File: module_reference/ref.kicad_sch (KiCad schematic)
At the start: 77 parts, among them Q201 BDP949, U201 ADR1000, U202 OPA2140, U203 ADA4523-1

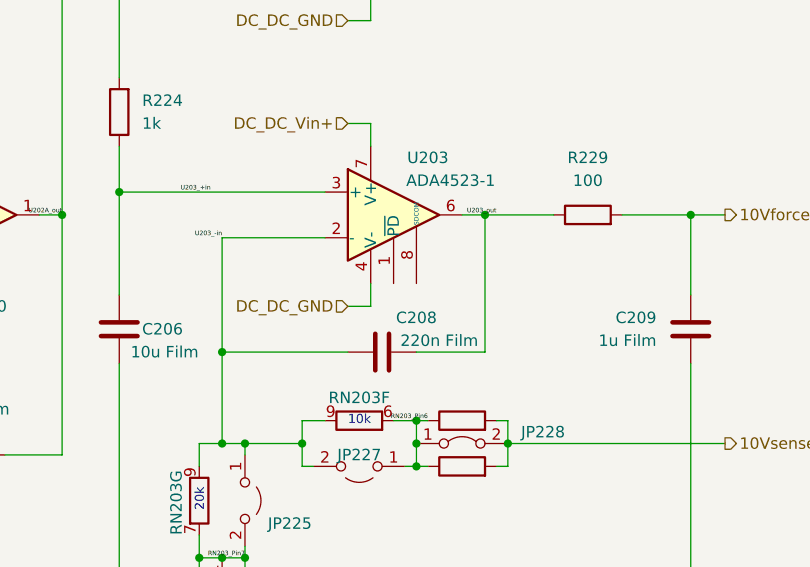
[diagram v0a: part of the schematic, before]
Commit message: backplane connector changes
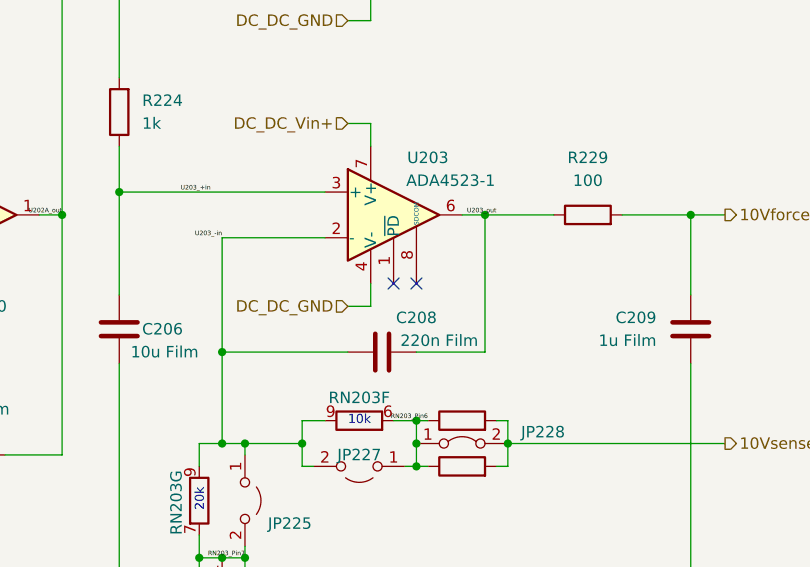
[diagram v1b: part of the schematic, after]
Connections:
- no-connect marks 0 -> 2
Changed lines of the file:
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@@
   (junction (at 107.95 106.68) (diameter 0) (color 0 0 0 0)
   )
+  (no_connect (at 223.52 76.2))
+  (no_connect (at 220.98 76.2))
   (wire (pts (xy 218.44 76.2) (xy 218.44 78.74))
     (stroke (width 0) (type default) (color 0 0 0 0))

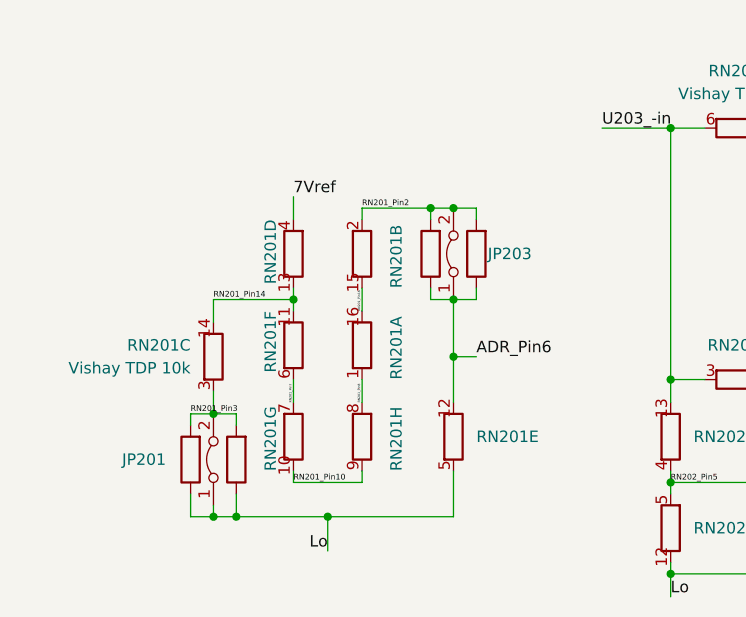
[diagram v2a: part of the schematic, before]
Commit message: started Rev. 0.4 with better 1k/12k divider
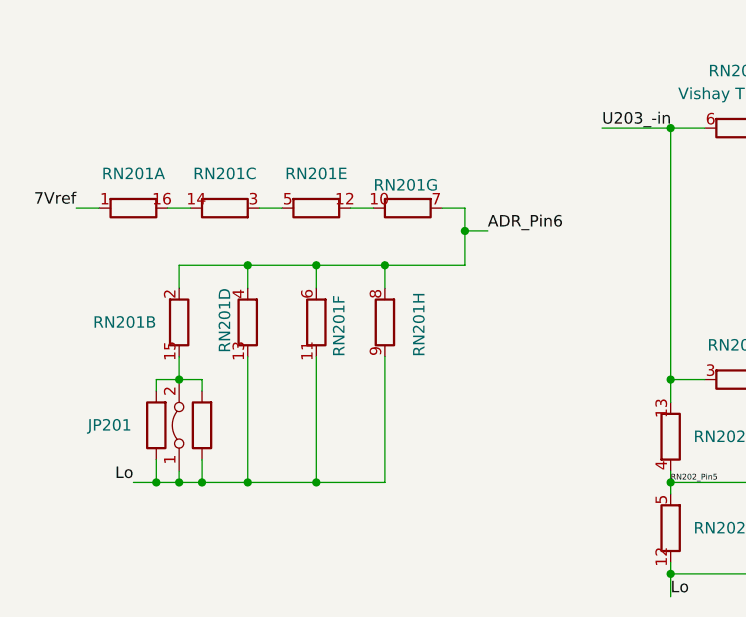
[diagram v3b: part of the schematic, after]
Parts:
- removed JP203: Jumper_2_Bridged, Jumper:SolderJumper-2_P1.3mm_Bridged_RoundedPad1.0x1.5mm, symbol Jumper:Jumper_2_Bridged
- removed R203: 0, Crystal:Crystal_HC52-U_Vertical, symbol Device:R
- removed R205: 0, Resistor_SMD:R_0805_2012Metric, symbol Device:R
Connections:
- net RN201_Pin2 is gone; now on net ADR_Pin6: RN201.2 (R2.1)
- net RN201_Pin7 is gone; now on net ADR_Pin6: RN201.6 (R6.1), RN201.7 (R7.1)
- net 7Vref: now also RN201.1 (R1.1); no longer RN201.4 (R4.1)
- net ADR_Pin6: now also RN201.4 (R4.1), RN201.8 (R8.1); no longer RN201.12 (R5.2)
- net Lo: now also RN201.11 (R6.2), RN201.13 (R4.2), RN201.9 (R8.2); no longer RN201.5 (R5.1)
- net RN201_Pin10: no longer names the net of RN201.10 (R7.2)
- net RN201_Pin10: now also RN201.12 (R5.2); no longer RN201.9 (R8.2)
- removed net RN201_Pin14: RN201.11 (R6.2), RN201.13 (R4.2), RN201.14 (R3.2)
- net RN201_Pin16: no longer names the net of RN201.15 (R2.2)
- net RN201_Pin16: now also JP201.2 (B), R201.2, R202.2; no longer RN201.16 (R1.2)
- removed net RN201_Pin3: JP201.2 (B), R201.2, R202.2, RN201.3 (R3.1)
- removed net RN201_Pin8: RN201.1 (R1.1), RN201.8 (R8.1)
- new net: RN201.3 (R3.1), RN201.5 (R5.1)
- new net: RN201.14 (R3.2), RN201.16 (R1.2)
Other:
- moved on the sheet: JP201, RN201A, RN201B, RN201C, RN201D, RN201E, RN201F, RN201G, RN201H

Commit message: rev 0.4 layout step
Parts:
- removed Q201: BDP949, Package_TO_SOT_SMD:SOT-223-3_TabPin2, symbol Device:Q_NPN_BCE
- added Q201: BD135, Package_TO_SOT_THT:TO-126-3_Vertical, symbol Transistor_BJT:BD135
- NT201: footprint NetTie:NetTie-2_SMD_Pad0.5mm -> NetTie:NetTie-2_SMD_Pad2.0mm
- renumbered JP204 to JP202, JP205 to JP203, JP206 to JP204, JP207 to JP205, JP208 to JP206, JP209 to JP207, JP210 to JP208, JP211 to JP209, JP212 to JP210, JP213 to JP211, JP214 to JP212, JP215 to JP213, JP216 to JP214, JP217 to JP215, JP218 to JP216, JP219 to JP217, JP220 to JP218, JP221 to JP219, JP222 to JP220, JP223 to JP221, JP224 to JP222, JP225 to JP223, JP226 to JP224, JP227 to JP225, JP228 to JP226, JP229 to JP227, R204 to R203, R206 to R204, R207 to R205, R208 to R206, R209 to R207, R210 to R208, R211 to R209, R212 to R210, R213 to R211, R214 to R212, R215 to R213, R216 to R214, R217 to R215, R218 to R216, R219 to R217, R220 to R218, R221 to R219, R222 to R220, R223 to R221, R224 to R222, R225 to R223, R226 to R224, R227 to R225, R228 to R226, R229 to R227
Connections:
- net DC_DC_Vin+: now also Q201.2 (C)
- net Q201_base: now also Q201.3 (B)
- net heater+: now also Q201.1 (E)
- net RN201_Pin10: now reaches RN201.10 (R7.2), RN201.12 (R5.2)
- net RN201_Pin15: now reaches JP201.2 (B), R201.2, R202.2, RN201.15 (R2.2)
- net RN201_Pin5: now reaches RN201.3 (R3.1), RN201.5 (R5.1)
- net RN201_Pin14: now reaches RN201.14 (R3.2), RN201.16 (R1.2)

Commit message: Battery module Rev 0.2
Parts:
- added JP?: Jumper_2_Bridged, Jumper:SolderJumper-2_P1.3mm_Bridged_RoundedPad1.0x1.5mm, symbol Jumper:Jumper_2_Bridged
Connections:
- net RN202_Pin14: now also JP?.2 (B)
- net RN202_Pin2: now also JP?.1 (A)
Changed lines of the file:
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@@
+    (stroke (width 0) (type default) (color 0 0 0 0))
+  )
+  (wire (pts (xy 114.3 167.64) (xy 115.57 167.64))
     (stroke (width 0) (type default) (color 0 0 0 0))
   )
@@
     (stroke (width 0) (type default) (color 0 0 0 0))
   )
+  (wire (pts (xy 115.57 162.56) (xy 115.57 167.64))
+    (stroke (width 0) (type default) (color 0 0 0 0))
+  )
   (wire (pts (xy 110.49 106.68) (xy 110.49 107.95))
     (stroke (width 0) (type default) (color 0 0 0 0))
@@
     (stroke (width 0) (type default) (color 0 0 0 0))
   )
+  (wire (pts (xy 102.87 167.64) (xy 104.14 167.64))
+    (stroke (width 0) (type default) (color 0 0 0 0))
+  )
   (wire (pts (xy 35.56 143.51) (xy 33.02 143.51))
     (stroke (width 0) (type default) (color 0 0 0 0))
@@
   )
   (wire (pts (xy 130.81 162.56) (xy 140.97 162.56))
+    (stroke (width 0) (type default) (color 0 0 0 0))
+  )
+  (wire (pts (xy 102.87 162.56) (xy 102.87 167.64))
     (stroke (width 0) (type default) (color 0 0 0 0))
   )
@@
       (effects (font (size 1.27 1.27)) hide)
     )
+    (pin "1")
+    (pin "2")
+  )
+  (symbol (lib_id "Jumper:Jumper_2_Bridged") (at 109.22 167.64 180) (unit 1)
+    (in_bom no) (on_board yes) (fields_autoplaced)
+    (property "Reference" "JP?" (id 0) (at 109.22 165.1 0))
+    (property "Value" "Jumper_2_Bridged" (id 1) (at 109.22 171.45 0)
+      (effects (font (size 1.27 1.27)) hide)
+    )
+    (property "Footprint" "Jumper:SolderJumper-2_P1.3mm_Bridged_RoundedPad1.0x1.5mm" (id 2) (at 109.22 167.64 0)
+      (effects (font (size 1.27 1.27)) hide)
+    )
+    (property "Datasheet" "~" (id 3) (at 109.22 167.64 0)
+      (effects (font (size 1.27 1.27)) hide)
+    )

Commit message: asdf
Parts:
- removed JP?: Jumper_2_Bridged, Jumper:SolderJumper-2_P1.3mm_Bridged_RoundedPad1.0x1.5mm, symbol Jumper:Jumper_2_Bridged
- renumbered JP204 to JP205, JP205 to JP206, JP206 to JP207, JP207 to JP208, JP208 to JP209, JP209 to JP210, JP210 to JP211, JP211 to JP212, JP212 to JP213, JP213 to JP214, JP214 to JP215, JP215 to JP216, JP216 to JP217, JP217 to JP218, JP218 to JP219, JP219 to JP220, JP220 to JP221, JP221 to JP222, JP222 to JP223, JP223 to JP224, JP224 to JP225, JP225 to JP226, JP226 to JP227, JP227 to JP228
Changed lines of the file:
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@@
-    (stroke (width 0) (type default) (color 0 0 0 0))
-  )
-  (wire (pts (xy 114.3 167.64) (xy 115.57 167.64))
     (stroke (width 0) (type default) (color 0 0 0 0))
   )
@@
     (stroke (width 0) (type default) (color 0 0 0 0))
   )
-  (wire (pts (xy 115.57 162.56) (xy 115.57 167.64))
-    (stroke (width 0) (type default) (color 0 0 0 0))
-  )
   (wire (pts (xy 110.49 106.68) (xy 110.49 107.95))
     (stroke (width 0) (type default) (color 0 0 0 0))
@@
     (stroke (width 0) (type default) (color 0 0 0 0))
   )
-  (wire (pts (xy 102.87 167.64) (xy 104.14 167.64))
-    (stroke (width 0) (type default) (color 0 0 0 0))
-  )
   (wire (pts (xy 35.56 143.51) (xy 33.02 143.51))
     (stroke (width 0) (type default) (color 0 0 0 0))
@@
   )
   (wire (pts (xy 130.81 162.56) (xy 140.97 162.56))
-    (stroke (width 0) (type default) (color 0 0 0 0))
-  )
-  (wire (pts (xy 102.87 162.56) (xy 102.87 167.64))
     (stroke (width 0) (type default) (color 0 0 0 0))
   )
@@
   (symbol (lib_id "Jumper:Jumper_2_Open") (at 123.19 184.15 180) (unit 1)
     (in_bom no) (on_board yes) (fields_autoplaced)
-    (property "Reference" "JP212" (id 0) (at 123.19 181.61 0))
+    (property "Reference" "JP213" (id 0) (at 123.19 181.61 0))
     (property "Value" "Jumper_2_Open" (id 1) (at 121.9201 186.69 90)
       (effects (font (size 1.27 1.27)) (justify left) hide)
@@
   (symbol (lib_id "Jumper:Jumper_2_Open") (at 118.11 59.69 270) (unit 1)
     (in_bom no) (on_board yes)
-    (property "Reference" "JP207" (id 0) (at 113.03 59.69 90)
+    (property "Reference" "JP208" (id 0) (at 113.03 59.69 90)
       (effects (font (size 1.27 1.27)) (justify left))
     )
@@
   (symbol (lib_id "Jumper:Jumper_2_Open") (at 110.49 100.33 270) (unit 1)
     (in_bom no) (on_board yes)
-    (property "Reference" "JP205" (id 0) (at 113.03 100.33 90)
+    (property "Reference" "JP206" (id 0) (at 113.03 100.33 90)
       (effects (font (size 1.27 1.27)) (justify left))
     )
@@
   (symbol (lib_id "Jumper:Jumper_2_Bridged") (at 228.6 93.98 0) (unit 1)
     (in_bom no) (on_board yes)
-    (property "Reference" "JP226" (id 0) (at 240.03 92.71 0)
+    (property "Reference" "JP227" (id 0) (at 240.03 92.71 0)
       (effects (font (size 1.27 1.27)) (justify right))
     )
@@
     (pin "2")
   )
-  (symbol (lib_id "Jumper:Jumper_2_Bridged") (at 109.22 167.64 180) (unit 1)
-    (in_bom no) (on_board yes) (fields_autoplaced)
-    (property "Reference" "JP?" (id 0) (at 109.22 165.1 0))
-    (property "Value" "Jumper_2_Bridged" (id 1) (at 109.22 171.45 0)
-      (effects (font (size 1.27 1.27)) hide)
-    )
-    (property "Footprint" "Jumper:SolderJumper-2_P1.3mm_Bridged_RoundedPad1.0x1.5mm" (id 2) (at 109.22 167.64 0)
-      (effects (font (size 1.27 1.27)) hide)
-    )
-    (property "Datasheet" "~" (id 3) (at 109.22 167.64 0)
-      (effects (font (size 1.27 1.27)) hide)
-    )
-    (pin "1")
-    (pin "2")
-  )
   (symbol (lib_id "Jumper:Jumper_2_Bridged") (at 201.93 111.76 270) (unit 1)
     (in_bom no) (on_board yes)
-    (property "Reference" "JP222" (id 0) (at 205.74 119.38 90)
+    (property "Reference" "JP223" (id 0) (at 205.74 119.38 90)
       (effects (font (size 1.27 1.27)) (justify right))
     )
@@
   (symbol (lib_id "Jumper:Jumper_2_Open") (at 199.39 139.7 270) (unit 1)
     (in_bom no) (on_board yes)
-    (property "Reference" "JP221" (id 0) (at 201.93 142.24 90)
+    (property "Reference" "JP222" (id 0) (at 201.93 142.24 90)
       (effects (font (size 1.27 1.27)) (justify left))
     )
@@
   (symbol (lib_id "Jumper:Jumper_2_Open") (at 217.17 96.52 180) (unit 1)
     (in_bom no) (on_board yes)
-    (property "Reference" "JP225" (id 0) (at 217.17 95.25 0))
+    (property "Reference" "JP226" (id 0) (at 217.17 95.25 0))
     (property "Value" "Jumper_2_Open" (id 1) (at 217.17 96.52 0)
       (effects (font (size 1.27 1.27)) hide)
@@
   (symbol (lib_id "Jumper:Jumper_2_Open") (at 208.28 154.94 270) (unit 1)
     (in_bom no) (on_board yes)
-    (property "Reference" "JP224" (id 0) (at 210.82 157.48 90)
+    (property "Reference" "JP225" (id 0) (at 210.82 157.48 90)
       (effects (font (size 1.27 1.27)) (justify left))
     )
@@
   (symbol (lib_id "Jumper:Jumper_2_Bridged") (at 130.81 48.26 90) (unit 1)
     (in_bom no) (on_board yes)
-    (property "Reference" "JP213" (id 0) (at 128.27 40.64 90)
+    (property "Reference" "JP214" (id 0) (at 128.27 40.64 90)
       (effects (font (size 1.27 1.27)) (justify right))
     )
@@
   (symbol (lib_id "Jumper:Jumper_2_Bridged") (at 130.81 142.24 270) (unit 1)
     (in_bom no) (on_board yes) (fields_autoplaced)
-    (property "Reference" "JP214" (id 0) (at 133.35 142.2399 90)
+    (property "Reference" "JP215" (id 0) (at 133.35 142.2399 90)
       (effects (font (size 1.27 1.27)) (justify left))
     )
@@
   (symbol (lib_id "Jumper:Jumper_2_Open") (at 115.57 142.24 270) (unit 1)
     (in_bom no) (on_board yes) (fields_autoplaced)
-    (property "Reference" "JP206" (id 0) (at 114.3 142.2399 90)
+    (property "Reference" "JP207" (id 0) (at 114.3 142.2399 90)
       (effects (font (size 1.27 1.27)) (justify right))
     )
@@
   (symbol (lib_id "Jumper:Jumper_2_Open") (at 134.62 100.33 90) (unit 1)
     (in_bom no) (on_board yes)
-    (property "Reference" "JP217" (id 0) (at 135.89 100.33 90)
+    (property "Reference" "JP218" (id 0) (at 135.89 100.33 90)
       (effects (font (size 1.27 1.27)) (justify right))
     )
@@
   (symbol (lib_id "Jumper:Jumper_2_Bridged") (at 243.84 139.7 270) (unit 1)
     (in_bom no) (on_board yes)
-    (property "Reference" "JP227" (id 0) (at 246.38 138.43 0)
+    (property "Reference" "JP228" (id 0) (at 246.38 138.43 0)
       (effects (font (size 1.27 1.27)) (justify left))
     )
@@
   (symbol (lib_id "Jumper:Jumper_2_Open") (at 133.35 59.69 270) (unit 1)
     (in_bom no) (on_board yes)
-    (property "Reference" "JP216" (id 0) (at 137.16 57.15 0)
+    (property "Reference" "JP217" (id 0) (at 137.16 57.15 0)
       (effects (font (size 1.27 1.27)) (justify left))
     )
@@
   (symbol (lib_id "Jumper:Jumper_2_Bridged") (at 123.19 162.56 180) (unit 1)
     (in_bom no) (on_board yes) (fields_autoplaced)
-    (property "Reference" "JP210" (id 0) (at 123.19 160.02 0))
+    (property "Reference" "JP211" (id 0) (at 123.19 160.02 0))
     (property "Value" "Jumper_2_Bridged" (id 1) (at 123.19 166.37 0)
       (effects (font (size 1.27 1.27)) hide)
@@
   (symbol (lib_id "Jumper:Jumper_2_Open") (at 123.19 173.99 180) (unit 1)
     (in_bom no) (on_board yes) (fields_autoplaced)
-    (property "Reference" "JP211" (id 0) (at 123.19 171.45 0))
+    (property "Reference" "JP212" (id 0) (at 123.19 171.45 0))
     (property "Value" "Jumper_2_Open" (id 1) (at 121.9201 176.53 90)
       (effects (font (size 1.27 1.27)) (justify left) hide)
@@
   (symbol (lib_id "Jumper:Jumper_2_Bridged") (at 132.08 111.76 270) (unit 1)
     (in_bom no) (on_board yes)
-    (property "Reference" "JP215" (id 0) (at 135.89 119.38 90)
+    (property "Reference" "JP216" (id 0) (at 135.89 119.38 90)
       (effects (font (size 1.27 1.27)) (justify right))
     )
@@
   (symbol (lib_id "Jumper:Jumper_2_Open") (at 110.49 74.93 270) (unit 1)
     (in_bom no) (on_board yes)
-    (property "Reference" "JP204" (id 0) (at 114.3 72.39 0)
+    (property "Reference" "JP205" (id 0) (at 114.3 72.39 0)
       (effects (font (size 1.27 1.27)) (justify left))
     )
@@
   (symbol (lib_id "Jumper:Jumper_2_Open") (at 204.47 100.33 270) (unit 1)
     (in_bom no) (on_board yes)
-    (property "Reference" "JP223" (id 0) (at 207.01 102.87 90)
+    (property "Reference" "JP224" (id 0) (at 207.01 102.87 90)
       (effects (font (size 1.27 1.27)) (justify left))
     )
@@
   (symbol (lib_id "Jumper:Jumper_2_Bridged") (at 154.94 48.26 90) (unit 1)
     (in_bom no) (on_board yes)
-    (property "Reference" "JP220" (id 0) (at 158.75 48.26 90)
+    (property "Reference" "JP221" (id 0) (at 158.75 48.26 90)
       (effects (font (size 1.27 1.27)) (justify right))
     )
@@
   (symbol (lib_id "Jumper:Jumper_2_Open") (at 151.13 142.24 270) (unit 1)
     (in_bom no) (on_board yes) (fields_autoplaced)
-    (property "Reference" "JP219" (id 0) (at 153.67 142.2399 90)
+    (property "Reference" "JP220" (id 0) (at 153.67 142.2399 90)
       (effects (font (size 1.27 1.27)) (justify left))
     )
@@
   (symbol (lib_id "Jumper:Jumper_2_Bridged") (at 140.97 142.24 270) (unit 1)
     (in_bom no) (on_board yes) (fields_autoplaced)
-    (property "Reference" "JP218" (id 0) (at 143.51 142.2399 90)
+    (property "Reference" "JP219" (id 0) (at 143.51 142.2399 90)
       (effects (font (size 1.27 1.27)) (justify left))
     )
@@
   (symbol (lib_id "Jumper:Jumper_2_Bridged") (at 120.65 48.26 90) (unit 1)
     (in_bom no) (on_board yes)
-    (property "Reference" "JP208" (id 0) (at 118.11 40.64 90)
+    (property "Reference" "JP209" (id 0) (at 118.11 40.64 90)
       (effects (font (size 1.27 1.27)) (justify right))
     )
@@
   (symbol (lib_id "Jumper:Jumper_2_Bridged") (at 123.19 134.62 180) (unit 1)
     (in_bom no) (on_board yes)
-    (property "Reference" "JP209" (id 0) (at 123.19 137.16 0))
+    (property "Reference" "JP210" (id 0) (at 123.19 137.16 0))
     (property "Value" "Jumper_2_Bridged" (id 1) (at 123.19 138.43 0)
       (effects (font (size 1.27 1.27)) hide)

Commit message: Reference board Rev 0.5 schematic
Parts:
- removed JP201, JP210, JP211, JP215, JP219: Jumper_2_Bridged, Jumper:SolderJumper-2_P1.3mm_Bridged_RoundedPad1.0x1.5mm, symbol Jumper:Jumper_2_Bridged
- removed JP212, JP213, JP222, JP225: Jumper_2_Open, Jumper:SolderJumper-2_P1.3mm_Open_RoundedPad1.0x1.5mm, symbol Jumper:Jumper_2_Open
- added J201, J202, J203, J204, J205, J206, J207, J208: Conn_01x01, Connector_Wire:SolderWire-0.1sqmm_1x01_D0.4mm_OD1mm, symbol Connector_Generic:Conn_01x01
- added JP201, JP214: Jumper_2_Open, Jumper:SolderJumper-2_P1.3mm_Open_RoundedPad1.0x1.5mm, symbol Jumper:Jumper_2_Open
- added JP218, JP220: Jumper_2_Bridged, Jumper:SolderJumper-2_P1.3mm_Bridged_RoundedPad1.0x1.5mm, symbol Jumper:Jumper_2_Bridged
- added R218: 30k, Resistor_SMD:R_0805_2012Metric, symbol Device:R
- added R222, R224: DNP, Resistor_SMD:R_0805_2012Metric, symbol Device:R
- added R223, R225: DNP, Crystal:Crystal_HC52-U_Vertical, symbol Device:R
- R201: footprint Crystal:Crystal_HC52-U_Vertical -> Resistor_SMD:R_0805_2012Metric
- R202: footprint Resistor_SMD:R_0805_2012Metric -> Crystal:Crystal_HC52-U_Vertical
- R221: renamed from R218; value 0 -> DNP
- R226: renamed from R220; value 0 -> DNP
- renumbered JP205 to JP204, JP206 to JP205, JP208 to JP206, JP209 to JP207, JP214 to JP208, JP216 to JP209, JP217 to JP210, JP218 to JP211, JP207 to JP212, JP221 to JP213, JP220 to JP215, JP223 to JP216, JP224 to JP217, JP226 to JP219, JP227 to JP221, JP228 to JP222, R221 to R220, R222 to R227, R223 to R228, R224 to R229, R225 to R230, R226 to R231, R227 to R232
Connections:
- net RN202_Pin5 is gone; now on net U203_-in: RN202.4 (R4.1), RN202.5 (R5.1)
- net RN202_Pin8 is gone; now on net U203_-in: RN202.8 (R8.1)
- net 10Vsense: now also RN202.10 (R7.2), RN202.12 (R5.2), RN202.13 (R4.2), RN202.15 (R2.2), RN202.16 (R1.2), JP214.1 (A); no longer JP212.1 (A), RN202.7 (R7.1)
- net 7Vref: now also JP218.1 (A)
- net ADR_Pin4: now also R218.1; no longer C205.2, U202.2 (-)
- net ADR_Pin5: now also R222.1, R223.2
- net ADR_Pin6: now also R201.1, R202.1, RN201.5 (R5.1), JP201.2 (B); no longer RN201.2 (R2.1), RN201.4 (R4.1)
- net RN201_Pin14: now also J201.1 (Pin_1); no longer RN201.16 (R1.2)
- net RN201_Pin15: now also RN201.16 (R1.2); no longer R201.2, R202.2
- net RN204_Pin11: now also JP220.2 (B)
- net RN204_Pin16: now also JP218.2 (B), JP220.1 (A)
- net U202A_out: now also R222.2, R223.1, R224.2, R225.1
- net U203_-in: now also JP212.1 (A), RN202.2 (R2.1), RN202.7 (R7.1); no longer RN202.13 (R4.2)
- net JP211_Pin1 renamed ADR_Pin7
- net ADR_Pin7: now also C203.1, C204.1, C206.2, C209.1, JP203.2 (B), JP209.2 (B), JP216.2 (B), NT201.2, R207.2, R209.2, R213.2, R215.2, R228.2, R229.2, RN201.10 (R7.2), RN201.9 (R8.2), RN202.11 (R6.2), RN202.14 (R3.2), RN204.13 (R4.2), U201.7 (GND)
- net JP221_Pin2 renamed JP214_Pin2
- net JP214_Pin2: now also JP214.2 (B)
- removed net Lo: C203.1, C204.1, C206.2, C209.1, JP203.2 (B), JP209.2 (B), JP216.2 (B), NT201.2, R201.1, R202.1, R207.2, R209.2, R213.2, R215.2, R228.2, R229.2, RN201.11 (R6.2), RN201.13 (R4.2), RN201.9 (R8.2), RN202.12 (R5.2), RN204.13 (R4.2), U201.7 (GND)
- net RN201_Pin10 renamed RN201_Pin12
- net RN201_Pin12: now also J207.1 (Pin_1); no longer RN201.10 (R7.2)
- net RN201_Pin5 renamed RN201_Pin3
- net RN201_Pin3: now also J205.1 (Pin_1); no longer RN201.5 (R5.1)
- net RN202_Pin1 renamed RN212_Pin2
- net RN212_Pin2: now also JP212.2 (B)
- removed net RN202_Pin14: RN202.10 (R7.2), RN202.11 (R6.2), RN202.14 (R3.2), RN202.15 (R2.2)
- net RN202_Pin16 renamed RN202_Pin9
- net RN202_Pin9: no longer RN202.16 (R1.2)
- removed net RN202_Pin2: JP212.2 (B), RN202.2 (R2.1)
- new net JP201_Pin1: J203.1 (Pin_1), JP201.1 (A), R201.2, R202.2
- new net RN201_Pin11: J208.1 (Pin_1), RN201.11 (R6.2)
- new net RN201_Pin13: J206.1 (Pin_1), RN201.13 (R4.2)
- new net RN201_Pin2: J204.1 (Pin_1), RN201.2 (R2.1)
- new net RN201_Pin4: J202.1 (Pin_1), RN201.4 (R4.1)
- new net U202A_-in: C205.2, R218.2, R224.1, R225.2, U202.2 (-)
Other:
- moved on the sheet: C201, C203, C204, C205, C206, C207, C208, C209, D201, D202, JP202, JP203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
